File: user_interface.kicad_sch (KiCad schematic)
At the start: 25 parts, among them J1201 Conn_01x08, J1202 5051104091, U1201 TCA9554PW, U1202 STLD40DPUR

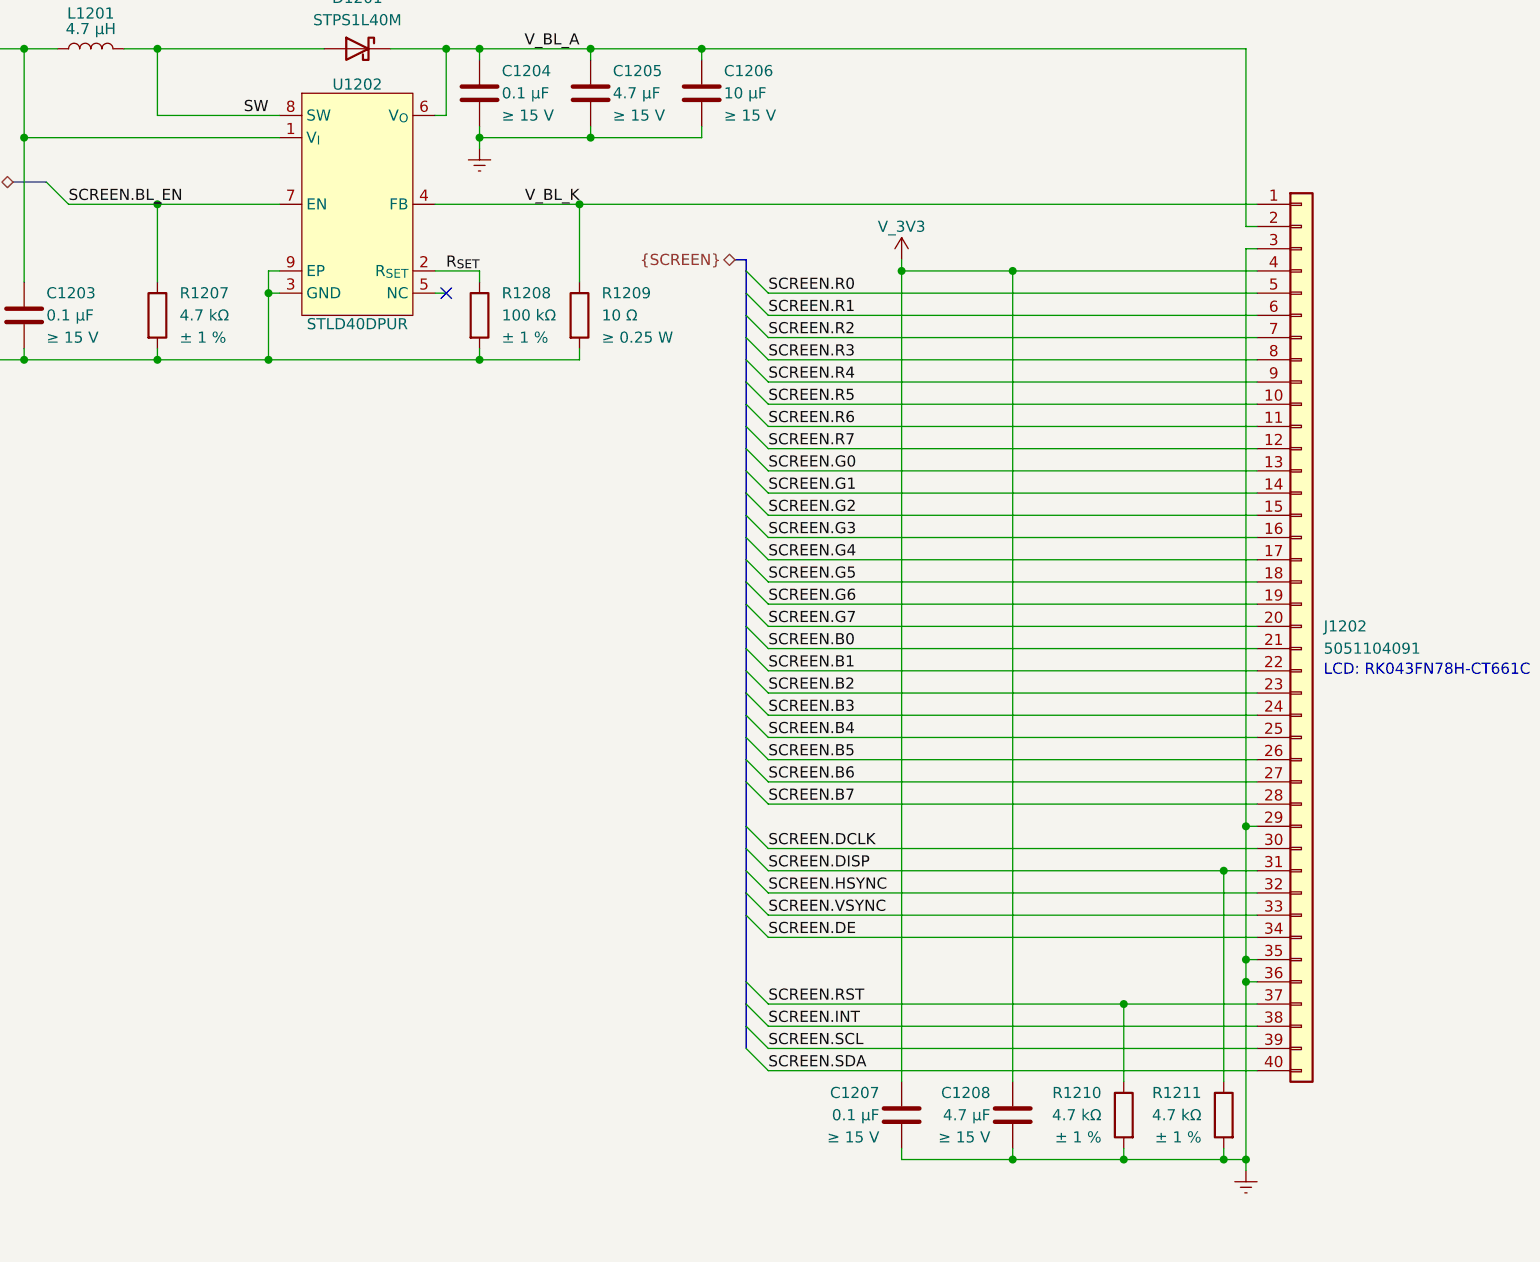
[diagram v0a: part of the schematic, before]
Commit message: Add series termination, refactor schematics
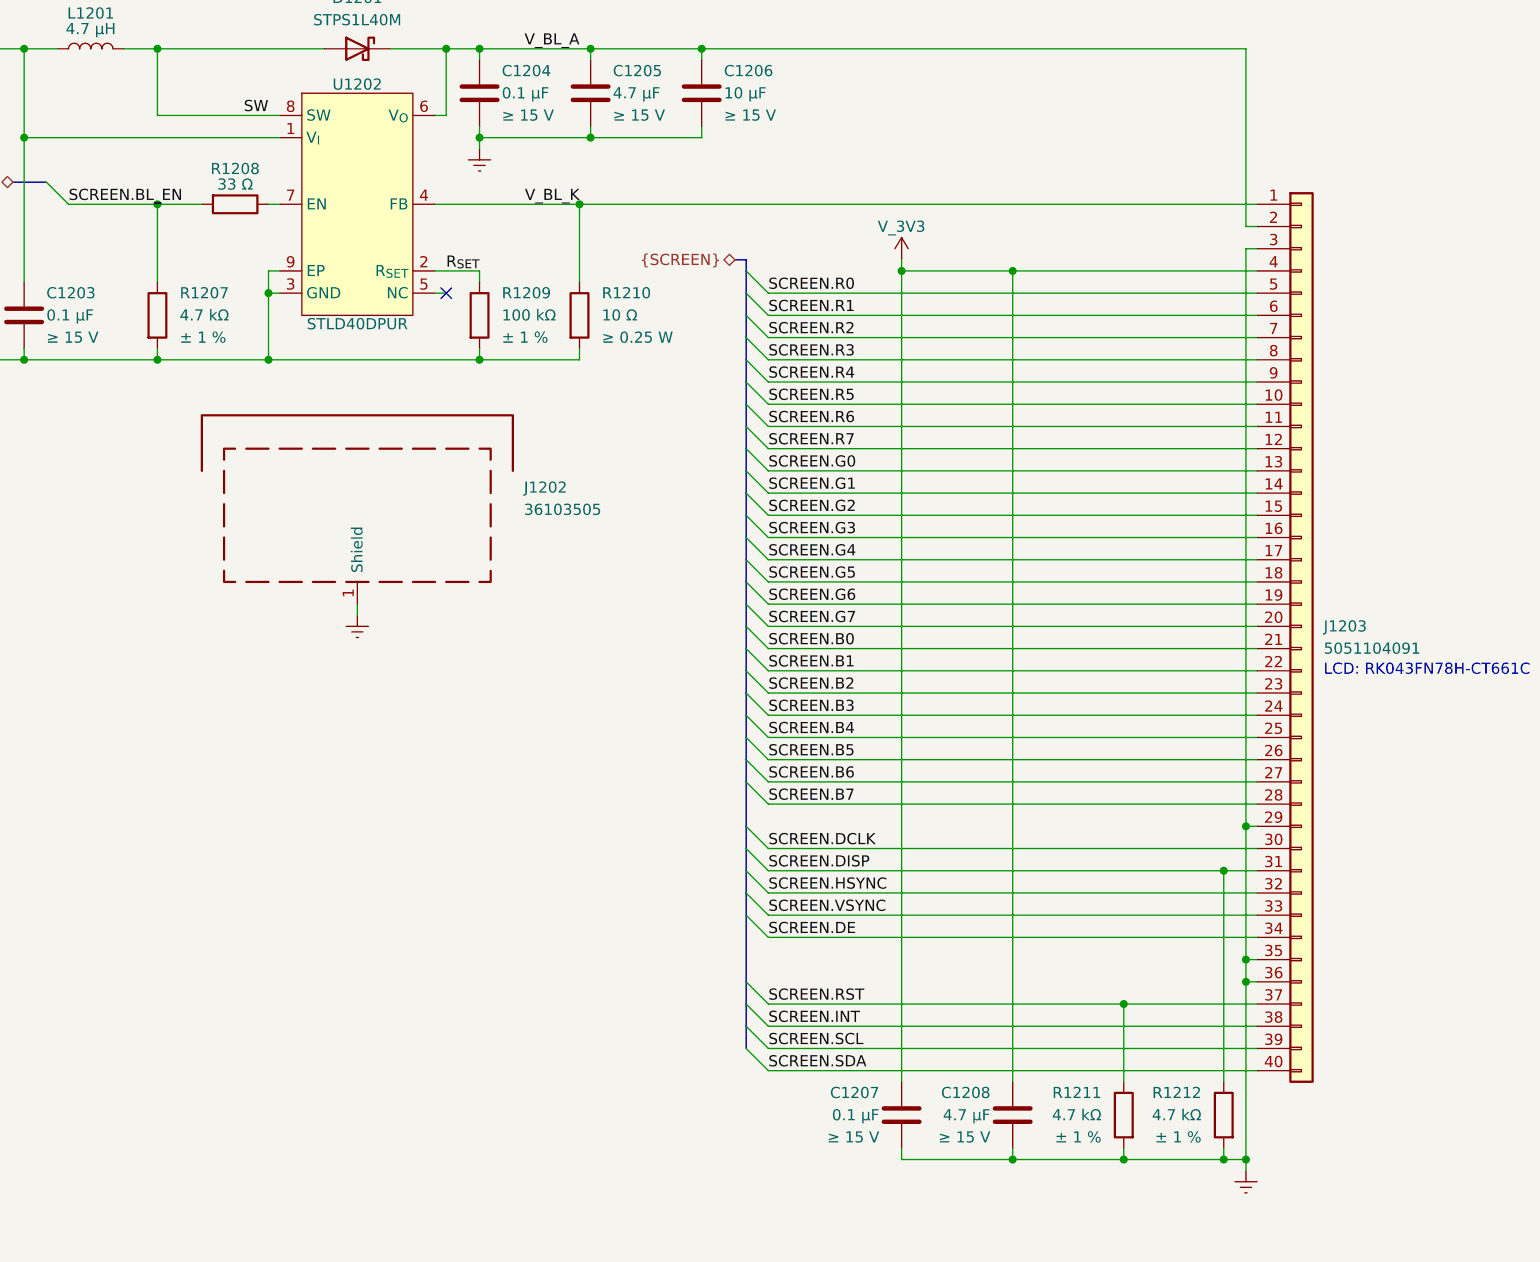
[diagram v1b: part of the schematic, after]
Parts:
- added J1202: 36103505, symbol Device:RFShield_TwoPieces
- added R1208: 33 Ω, perfect_footprints:R_0402_1005Metric, symbol Device:R
- renumbered J1202 to J1203, R1208 to R1209, R1209 to R1210, R1210 to R1211, R1211 to R1212
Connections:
- net GND: now also J1202.1 (Shield)
- net SCREEN.BL_EN: now also R1208.2; no longer U1202.7 (EN)
- new net: R1208.1, U1202.7 (EN)

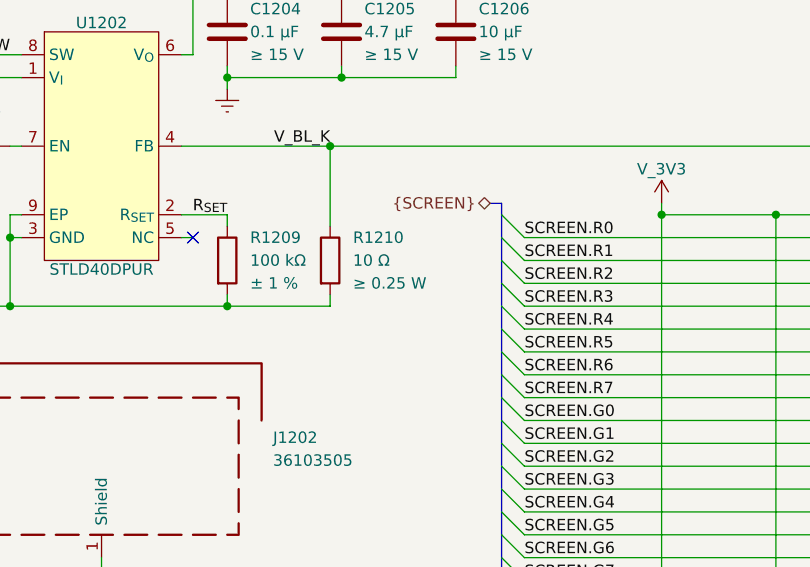
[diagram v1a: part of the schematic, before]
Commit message: Refactor symbol properties
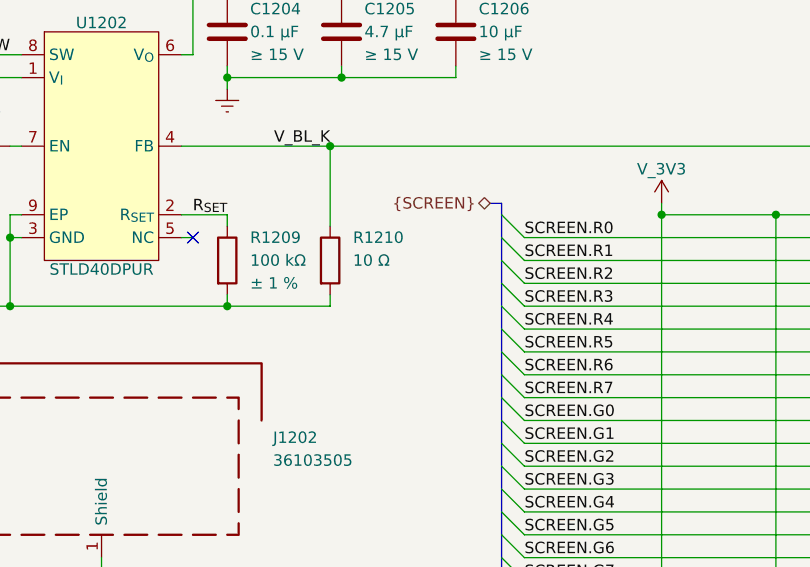
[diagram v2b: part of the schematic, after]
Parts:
- C1201, C1205, C1208: DigiKey Part Number 490-7205-1-ND -> (none)
- R1203, R1204, R1205, R1206, R1208: DigiKey Part Number 732-560112110020CT-ND -> (none)
- R1209: DigiKey Part Number 732-560112110019CT-ND -> (none)
- R1210: Power ≥ 0.25 W -> (none); Power rating (none) -> ≥ 0.25 W

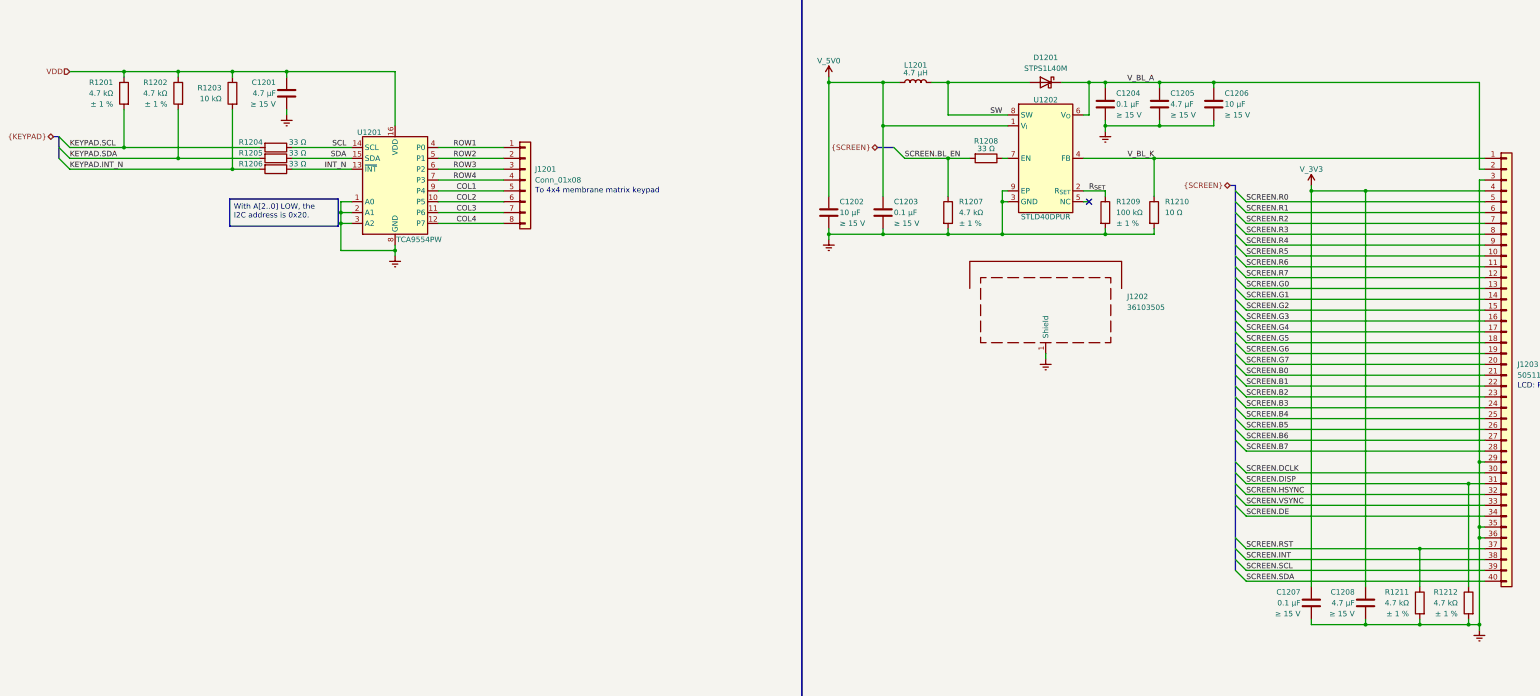
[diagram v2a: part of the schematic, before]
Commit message: Refactor SDMMC, UI, Wirelessg
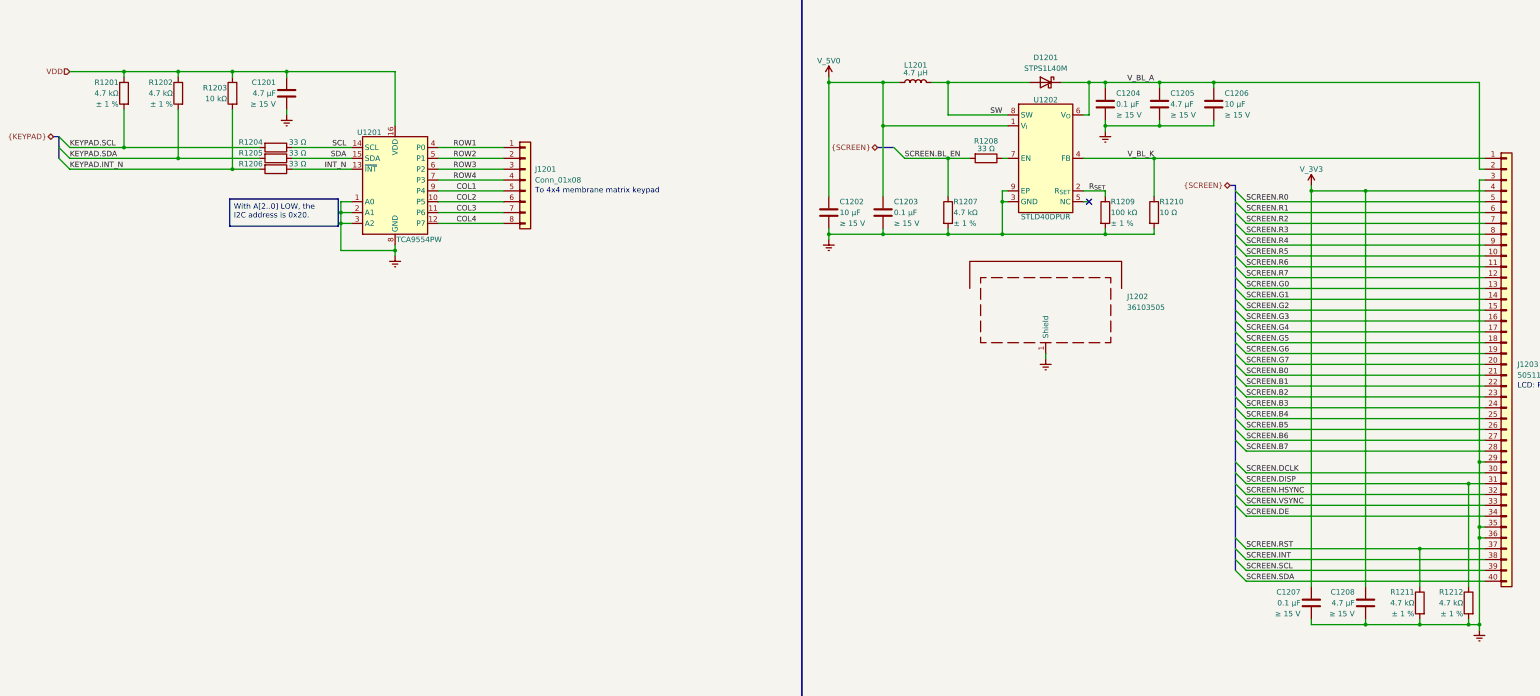
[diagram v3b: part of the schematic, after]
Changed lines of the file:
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@@
 		(dnp no)
 		(property "Reference" "R1203"
-			(at 73.66 105.4099 0)
+			(at 74.93 105.41 0)
 			(effects
 				(font
@@
 		)
 		(property "Value" "10 kΩ"
-			(at 73.66 107.9499 0)
+			(at 74.93 107.95 0)
 			(effects
 				(font
@@
 		(dnp no)
 		(property "Reference" "R1211"
-			(at 351.79 223.52 0)
+			(at 353.06 223.52 0)
 			(effects
 				(font
@@
 		)
 		(property "Value" "4.7 kΩ"
-			(at 351.79 226.06 0)
+			(at 353.06 226.06 0)
 			(effects
 				(font
@@
 		)
 		(property "Tolerance" "± 1 %"
-			(at 351.79 228.6001 0)
+			(at 353.06 228.6001 0)
 			(effects
 				(font
@@
 		(dnp no)
 		(property "Reference" "R1209"
-			(at 283.21 132.08 0)
+			(at 281.94 132.08 0)
 			(effects
 				(font
@@
 		)
 		(property "Value" "100 kΩ"
-			(at 283.21 134.62 0)
+			(at 281.94 134.62 0)
 			(effects
 				(font
@@
 		)
 		(property "Tolerance" "± 1 %"
-			(at 283.21 137.1601 0)
+			(at 281.94 137.1601 0)
 			(effects
 				(font
@@
 		(dnp no)
 		(property "Reference" "R1201"
-			(at 48.26 104.14 0)
+			(at 49.53 104.1401 0)
 			(effects
 				(font
@@
 		)
 		(property "Value" "4.7 kΩ"
-			(at 48.26 106.68 0)
+			(at 49.53 106.6801 0)
 			(effects
 				(font
@@
 		)
 		(property "Tolerance" "± 1 %"
-			(at 48.26 109.2201 0)
+			(at 49.53 109.2202 0)
 			(effects
 				(font
@@
 		(dnp no)
 		(property "Reference" "R1210"
-			(at 294.64 132.08 0)
+			(at 293.37 132.08 0)
 			(effects
 				(font
@@
 		)
 		(property "Value" "10 Ω"
-			(at 294.64 134.62 0)
+			(at 293.37 134.62 0)
 			(effects
 				(font
@@
 		(dnp no)
 		(property "Reference" "R1202"
-			(at 60.96 104.14 0)
+			(at 62.23 104.1401 0)
 			(effects
 				(font
@@
 		)
 		(property "Value" "4.7 kΩ"
-			(at 60.96 106.68 0)
+			(at 62.23 106.6801 0)
 			(effects
 				(font
@@
 		)
 		(property "Tolerance" "± 1 %"
-			(at 60.96 109.2201 0)
+			(at 62.23 109.2202 0)
 			(effects
 				(font
@@
 		(dnp no)
 		(property "Reference" "R1207"
-			(at 246.38 132.08 0)
+			(at 245.11 132.08 0)
 			(effects
 				(font
@@
 		)
 		(property "Value" "4.7 kΩ"
-			(at 246.38 134.62 0)
+			(at 245.11 134.62 0)
 			(effects
 				(font
@@
 		)
 		(property "Tolerance" "± 1 %"
-			(at 246.38 137.1601 0)
+			(at 245.11 137.1601 0)
 			(effects
 				(font
@@
 		(dnp no)
 		(property "Reference" "R1212"
-			(at 363.22 223.52 0)
+			(at 364.49 223.52 0)
 			(effects
 				(font
@@
 		)
 		(property "Value" "4.7 kΩ"
-			(at 363.22 226.06 0)
+			(at 364.49 226.06 0)
 			(effects
 				(font
@@
 		)
 		(property "Tolerance" "± 1 %"
-			(at 363.22 228.6001 0)
-			(effects
-				(font
+			(at 364.49 228.6001 0)
+			(effects
+				(font
